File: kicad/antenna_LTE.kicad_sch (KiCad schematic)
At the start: 2 parts, among them J9 SMA_CONNECTOR

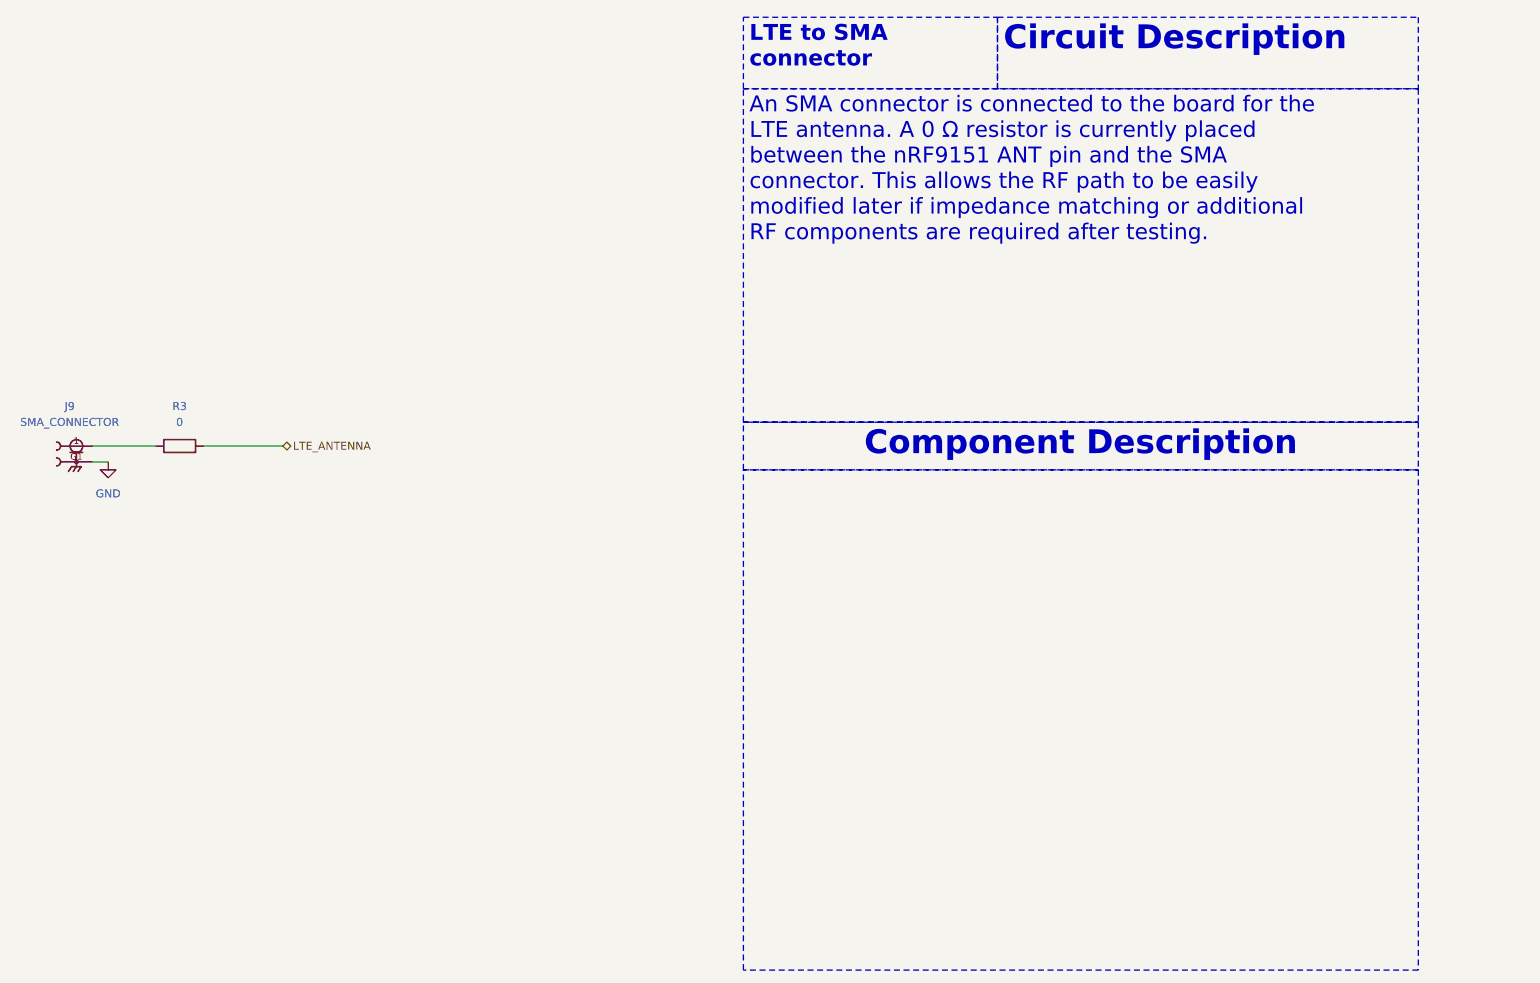
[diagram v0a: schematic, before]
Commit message: feat: update GNSS circuit
Signed-off-by: Bobo Bäck Engström <bobo@id8-engineering.io>
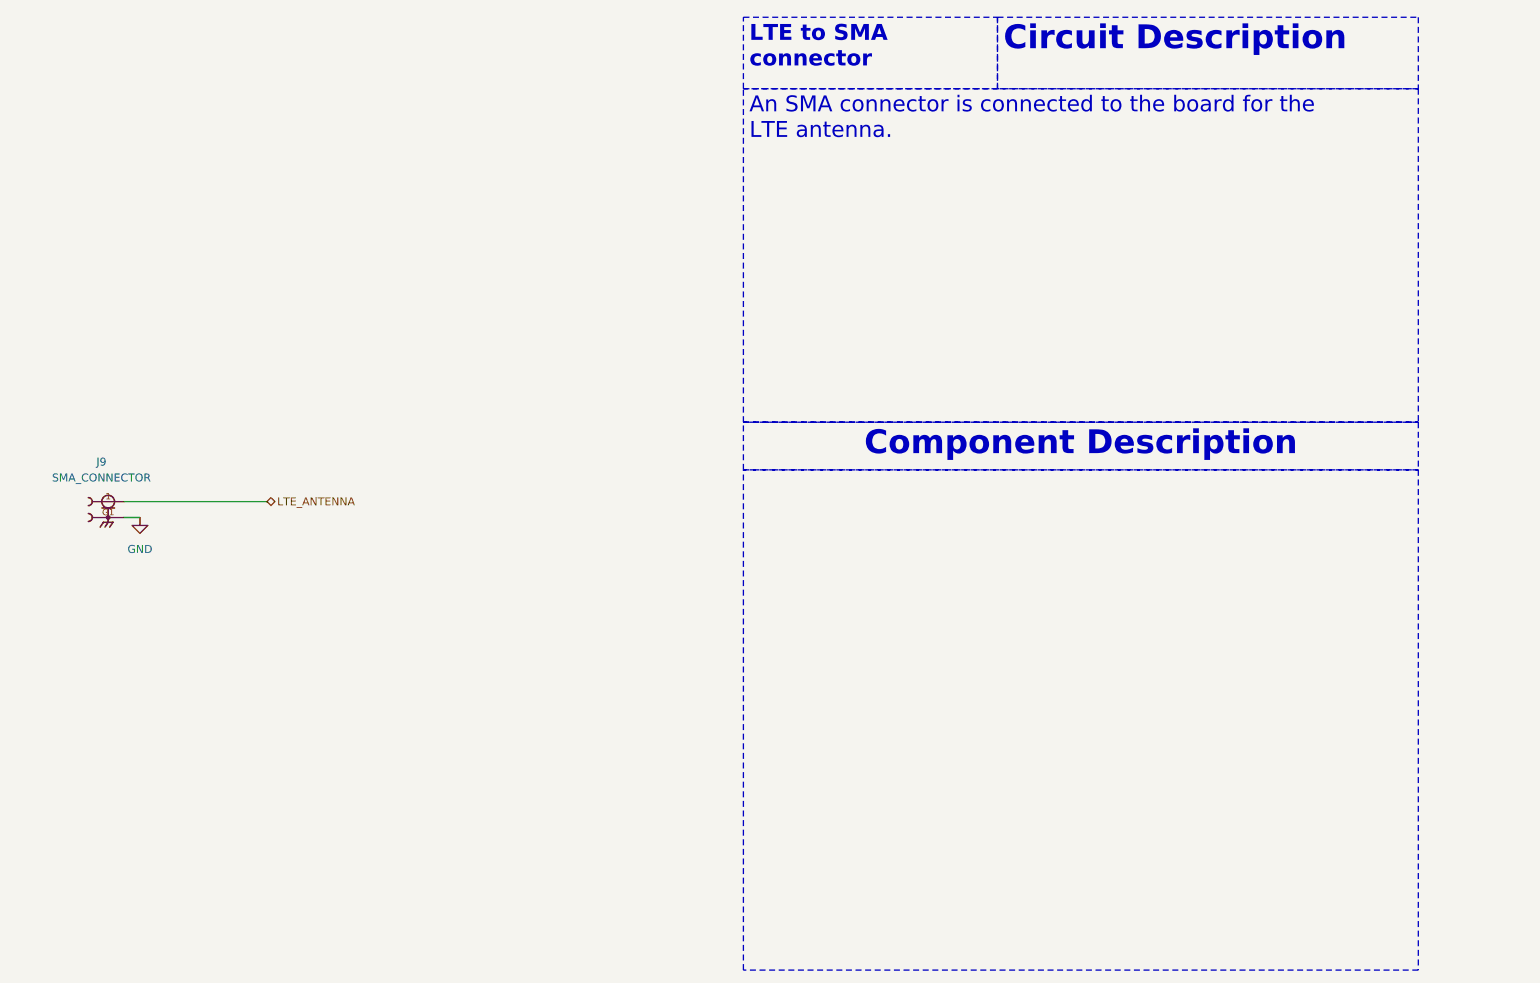
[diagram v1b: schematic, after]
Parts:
- removed R3: 0, seven-lib:R_0603_1608Metric, symbol seven_lib:R
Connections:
- net LTE_ANTENNA: now also J9.1
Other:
- moved on the sheet: J9
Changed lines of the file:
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@@
 		)
 	)
-	(text_box "An SMA connector is connected to the board for the LTE antenna. A 0 Ω resistor is currently placed between the nRF9151 ANT pin and the SMA connector. This allows the RF path to be easily modified later if impedance matching or additional RF components are required after testing."
+	(text_box "An SMA connector is connected to the board for the LTE antenna."
 		(exclude_from_sim no)
 		(at 176.53 24.13 0)
@@
 	(wire
 		(pts
-			(xy 72.39 81.28) (xy 82.55 81.28)
+			(xy 77.47 90.17) (xy 100.33 90.17)
 		)
 		(stroke
@@
 	(wire
 		(pts
-			(xy 90.17 81.28) (xy 102.87 81.28)
-		)
-		(stroke
-			(width 0)
-			(type default)
-		)
-	)
-	(wire
-		(pts
-			(xy 74.93 83.82) (xy 72.39 83.82)
+			(xy 80.01 92.71) (xy 77.47 92.71)
 		)
 		(stroke
@@
 	(hierarchical_label "LTE_ANTENNA"
 		(shape bidirectional)
-		(at 102.87 81.28 0)
+		(at 100.33 90.17 0)
 		(effects
 			(font
@@
 	(symbol
 		(lib_id "seven_lib:SMA_CONNECTOR")
-		(at 69.85 81.28 0)
+		(at 74.93 90.17 0)
 		(unit 1)
 		(exclude_from_sim no)
@@
 		(fields_autoplaced yes)
 		(property "Reference" "J9"
-			(at 68.7705 74.93 0)
+			(at 73.8505 83.82 0)
 			(effects
 				(font
@@
 		)
 		(property "Value" "SMA_CONNECTOR"
-			(at 68.7705 77.47 0)
+			(at 73.8505 86.36 0)
 			(effects
 				(font
@@
 		)
 		(property "Footprint" "seven-lib:LPRS_SMA_CONNECTOR"
-			(at 69.85 81.28 0)
+			(at 74.93 90.17 0)
 			(effects
 				(font
@@
 		)
 		(property "Datasheet" ""
-			(at 69.85 81.28 0)
+			(at 74.93 90.17 0)
 			(effects
 				(font
@@
 		)
 		(property "Description" ""
-			(at 69.85 81.28 0)
+			(at 74.93 90.17 0)
 			(effects
 				(font
@@
 		)
 		(property "MF" "LPRS"
-			(at 69.85 81.28 0)
+			(at 74.93 90.17 0)
 			(effects
 				(font
@@
 		)
 		(property "MAXIMUM_PACKAGE_HEIGHT" "8.3 mm"
-			(at 69.85 81.28 0)
+			(at 74.93 90.17 0)
 			(effects
 				(font
@@
 		)
 		(property "Package" "None"
-			(at 69.85 81.28 0)
+			(at 74.93 90.17 0)
 			(effects
 				(font
@@
 		)
 		(property "Price" "None"
-			(at 69.85 81.28 0)
+			(at 74.93 90.17 0)
 			(effects
 				(font
@@
 		)
 		(property "Check_prices" "https://www.snapeda.com/parts/SMA%20CONNECTOR/LPRS/view-part/?ref=eda"
-			(at 69.85 81.28 0)
+			(at 74.93 90.17 0)
 			(effects
 				(font
@@
 		)
 		(property "STANDARD" "Manufacturer Recommendations"
-			(at 69.85 81.28 0)
+			(at 74.93 90.17 0)
 			(effects
 				(font
@@
 		)
 		(property "PARTREV" "1.3"
-			(at 69.85 81.28 0)
+			(at 74.93 90.17 0)
 			(effects
 				(font
@@
 		)
 		(property "SnapEDA_Link" "https://www.snapeda.com/parts/SMA%20CONNECTOR/LPRS/view-part/?ref=snap"
-			(at 69.85 81.28 0)
+			(at 74.93 90.17 0)
 			(effects
 				(font
@@
 		)
 		(property "MP" "SMA CONNECTOR"
-			(at 69.85 81.28 0)
+			(at 74.93 90.17 0)
 			(effects
 				(font
@@
 		)
 		(property "Purchase-URL" "https://www.snapeda.com/api/url_track_click_mouser/?unipart_id=4703486&manufacturer=LPRS&part_name=SMA CONNECTOR&search_term=None"
-			(at 69.85 81.28 0)
+			(at 74.93 90.17 0)
 			(effects
 				(font
@@
 		)
 		(property "Description_1" "RF Coaxial Straight SMA Connector"
-			(at 69.85 81.28 0)
+			(at 74.93 90.17 0)
 			(effects
 				(font
@@
 		)
 		(property "Availability" "In Stock"
-			(at 69.85 81.28 0)
+			(at 74.93 90.17 0)
 			(effects
 				(font
@@
 		)
 		(property "MANUFACTURER" "LPRS"
-			(at 69.85 81.28 0)
+			(at 74.93 90.17 0)
 			(effects
 				(font
@@
 	)
 	(symbol
-		(lib_id "seven_lib:R")
-		(at 86.36 81.28 90)
-		(unit 1)
-		(exclude_from_sim no)
-		(in_bom yes)
-		(on_board yes)
-		(dnp no)
-		(fields_autoplaced yes)
-		(property "Reference" "R3"
-			(at 86.36 74.93 90)
-			(effects
-				(font
-					(size 1.27 1.27)
-				)
-			)
-		)
-		(property "Value" "0"
-			(at 86.36 77.47 90)
-			(effects
-				(font
-					(size 1.27 1.27)
-				)
-			)
-		)
-		(property "Footprint" "seven-lib:R_0603_1608Metric"
-			(at 86.36 83.058 90)
-			(effects
-				(font
-					(size 1.27 1.27)
-				)
-				(hide yes)
-			)
-		)
-		(property "Datasheet" "~"
-			(at 86.36 81.28 0)
-			(effects
-				(font
-					(size 1.27 1.27)
-				)
-				(hide yes)
-			)
-		)
-		(property "Description" "Resistor"
-			(at 86.36 81.28 0)
-			(effects
-				(font
-					(size 1.27 1.27)
-				)
-				(hide yes)
-			)
-		)
-		(pin "1"
-		)
-		(pin "2"
-		)
-		(instances
-			(project ""
-				(path "/8e3cc843-5797-49f3-8b3a-1c11450ccd1e/0b138663-1828-401e-979e-c711580e91a6"
-					(reference "R3")
-					(unit 1)
-				)
-			)
-		)
-	)
-	(symbol
 		(lib_id "seven_lib:GND")
-		(at 74.93 83.82 0)
+		(at 80.01 92.71 0)
 		(unit 1)
 		(exclude_from_sim no)
@@
 		(fields_autoplaced yes)
 		(property "Reference" "#PWR018"
-			(at 74.93 90.17 0)
+			(at 80.01 99.06 0)
 			(effects
 				(font
@@
 		)
 		(property "Value" "GND"
-			(at 74.93 88.9 0)
+			(at 80.01 97.79 0)
 			(effects
 				(font
@@
 		)
 		(property "Footprint" ""
-			(at 74.93 83.82 0)
+			(at 80.01 92.71 0)
 			(effects
 				(font
@@
 		)
 		(property "Datasheet" ""
-			(at 74.93 83.82 0)
+			(at 80.01 92.71 0)
 			(effects
 				(font
@@
 		)
 		(property "Description" "Power symbol creates a global label with name \"GND\" , ground"
-			(at 74.93 83.82 0)
-			(effects
-				(font
+			(at 80.01 92.71 0)
+			(effects
+				(font

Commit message: docs: update documentation to be more accurate
Signed-off-by: Bobo Bäck Engström <bobo@id8-engineering.io>
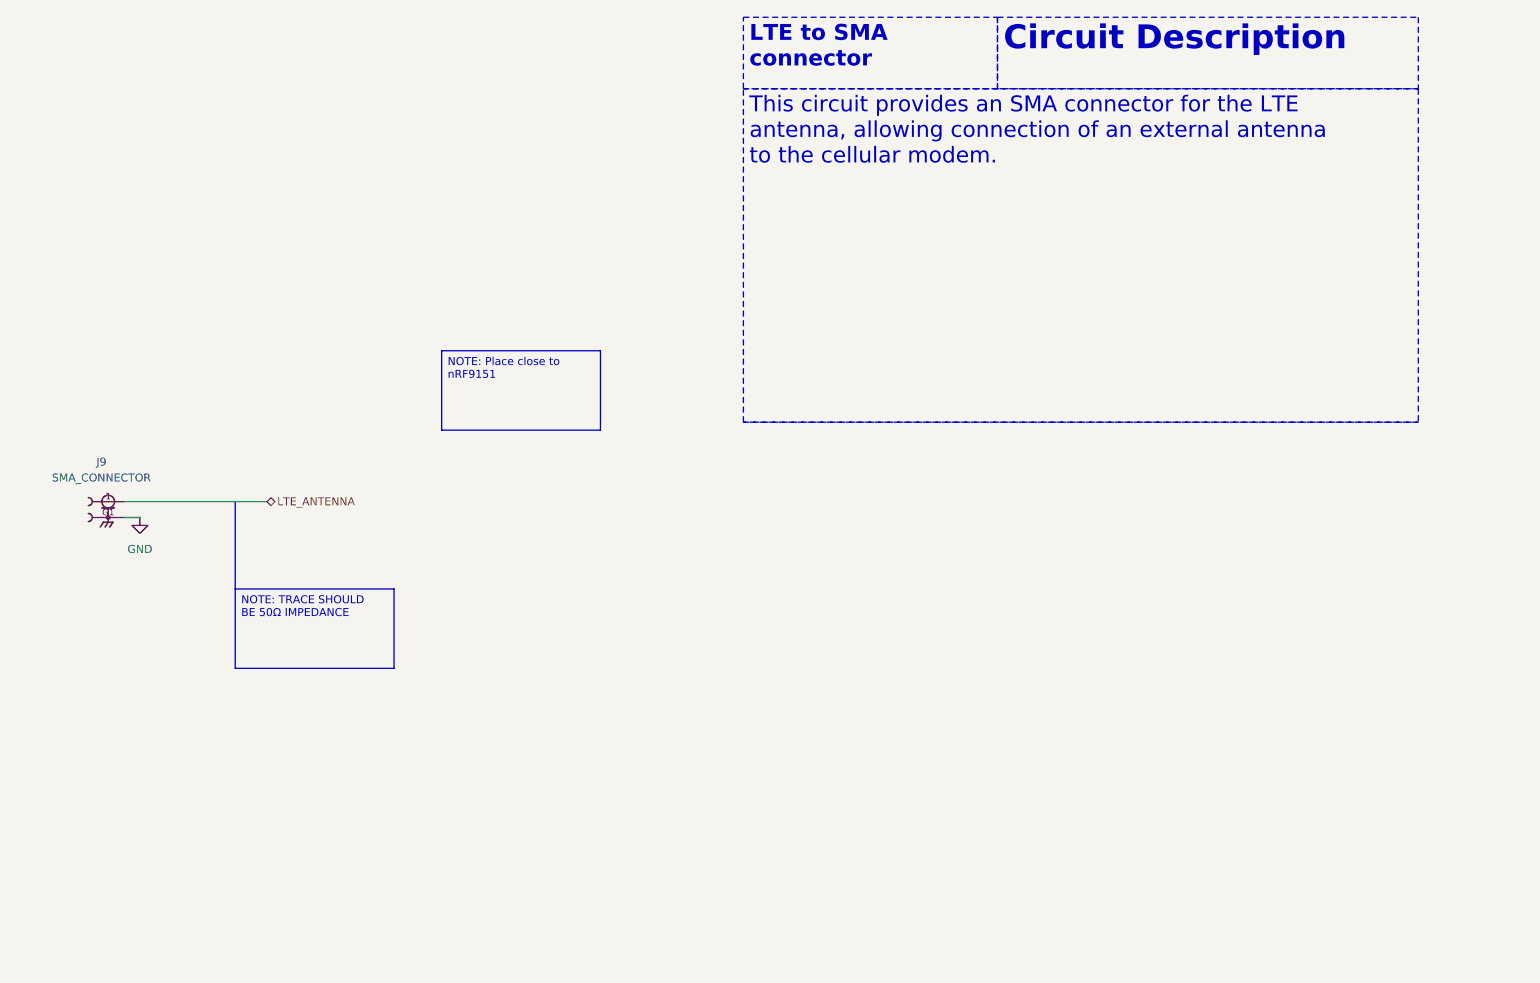
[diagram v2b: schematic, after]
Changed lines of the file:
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@@
+		)
+	)
+	(text_box "NOTE: TRACE SHOULD BE 50Ω IMPEDANCE\n"
+		(exclude_from_sim no)
+		(at 95.25 104.14 0)
+		(size 25.4 12.7)
+		(margins 0.9525 0.9525 0.9525 0.9525)
+		(stroke
+			(width 0)
+			(type solid)
+			(color 255 0 0 1)
+		)
+		(fill
+			(type color)
+			(color 255 67 78 1)
+		)
+		(effects
+			(font
+				(size 1.27 1.27)
+				(color 0 0 0 1)
+			)
+			(justify left top)
 		)
 	)
@@
 		)
 	)
-	(text_box "An SMA connector is connected to the board for the LTE antenna."
+	(text_box "This circuit provides an SMA connector for the LTE antenna, allowing connection of an external antenna to the cellular modem."
 		(exclude_from_sim no)
 		(at 176.53 24.13 0)
@@
 		)
 	)
-	(text_box "\n"
+	(text_box "NOTE: Place close to nRF9151"
 		(exclude_from_sim no)
-		(at 176.53 85.09 0)
-		(size 107.95 80.01)
+		(at 128.27 66.04 0)
+		(size 25.4 12.7)
 		(margins 0.9525 0.9525 0.9525 0.9525)
 		(stroke
 			(width 0)
-			(type dash)
+			(type solid)
+			(color 255 0 0 1)
 		)
 		(fill
-			(type none)
+			(type color)
+			(color 255 67 78 1)
 		)
 		(effects
 			(font
-				(size 2.54 2.54)
+				(size 1.27 1.27)
+				(color 0 0 0 1)
 			)
 			(justify left top)
-		)
-	)
-	(text_box "Component Description\n"
-		(exclude_from_sim no)
-		(at 176.53 77.47 0)
-		(size 107.95 7.62)
-		(margins 0.9525 0.9525 0.9525 0.9525)
-		(stroke
-			(width 0)
-			(type dash)
-		)
-		(fill
-			(type none)
-		)
-		(effects
-			(font
-				(size 3.81 3.81)
-				(thickness 0.762)
-				(bold yes)
-			)
-			(justify top)
 		)
 	)
@@
 		)
 	)
+	(polyline
+		(pts
+			(xy 95.25 90.17) (xy 95.25 104.14)
+		)
+		(stroke
+			(width 0)
+			(type default)
+		)
+	)

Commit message: fix: changes made according to review meeting
Signed-off-by: Bobo Bäck Engström <bobo@id8-engineering.io>
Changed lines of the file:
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@@
 		)
 	)
-	(text_box "NOTE: TRACE SHOULD BE 50Ω IMPEDANCE\n"
+	(text_box "Note: The trace should have a characteristic impedance of 50 Ω."
 		(exclude_from_sim no)
 		(at 95.25 104.14 0)
@@
 		)
 	)
-	(text_box "NOTE: Place close to nRF9151"
+	(text_box "Note: Place SMA close to the nRF9151."
 		(exclude_from_sim no)
 		(at 128.27 66.04 0)
